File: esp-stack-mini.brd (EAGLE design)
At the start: 53.6 x 54.9 mm, 43 parts, among them IC1 FT232RL, Q1 200mA/50V, U1 TPS737XX, U2 MCP73831

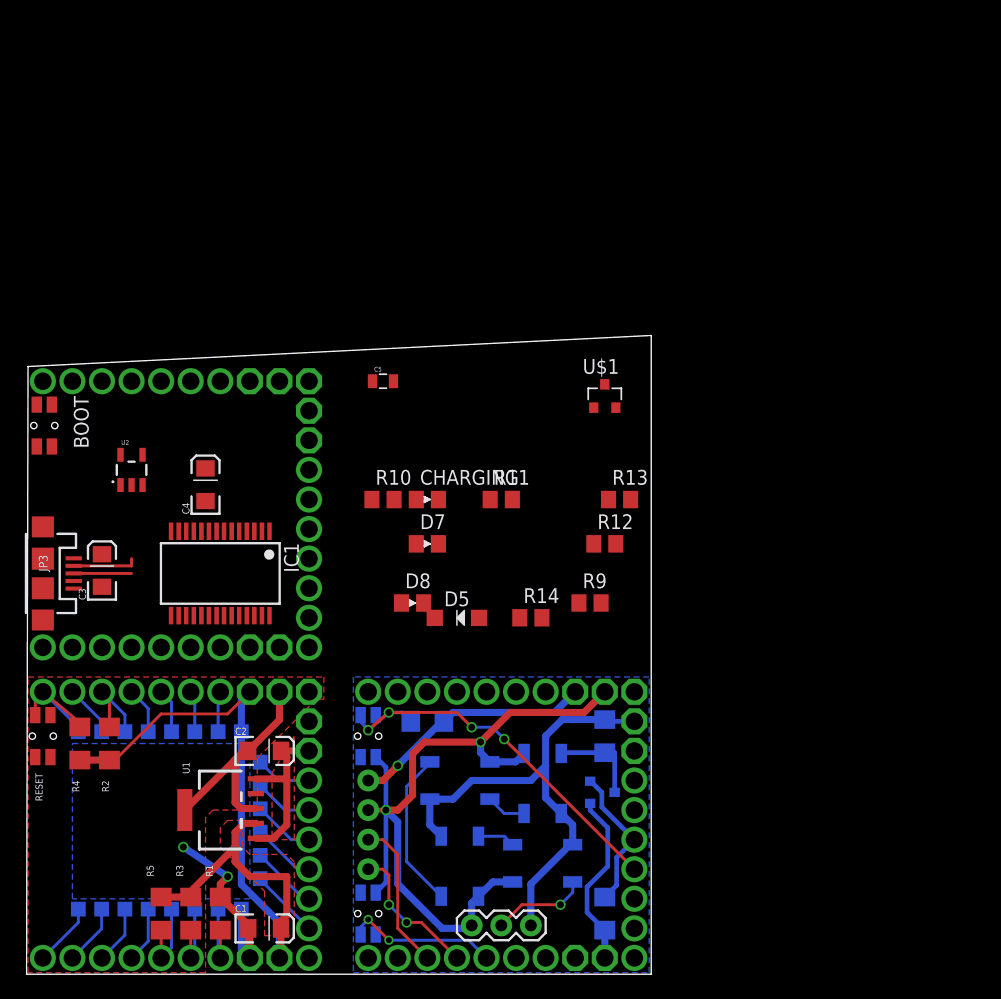
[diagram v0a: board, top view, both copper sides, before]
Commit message: USB/Battery board all-connected
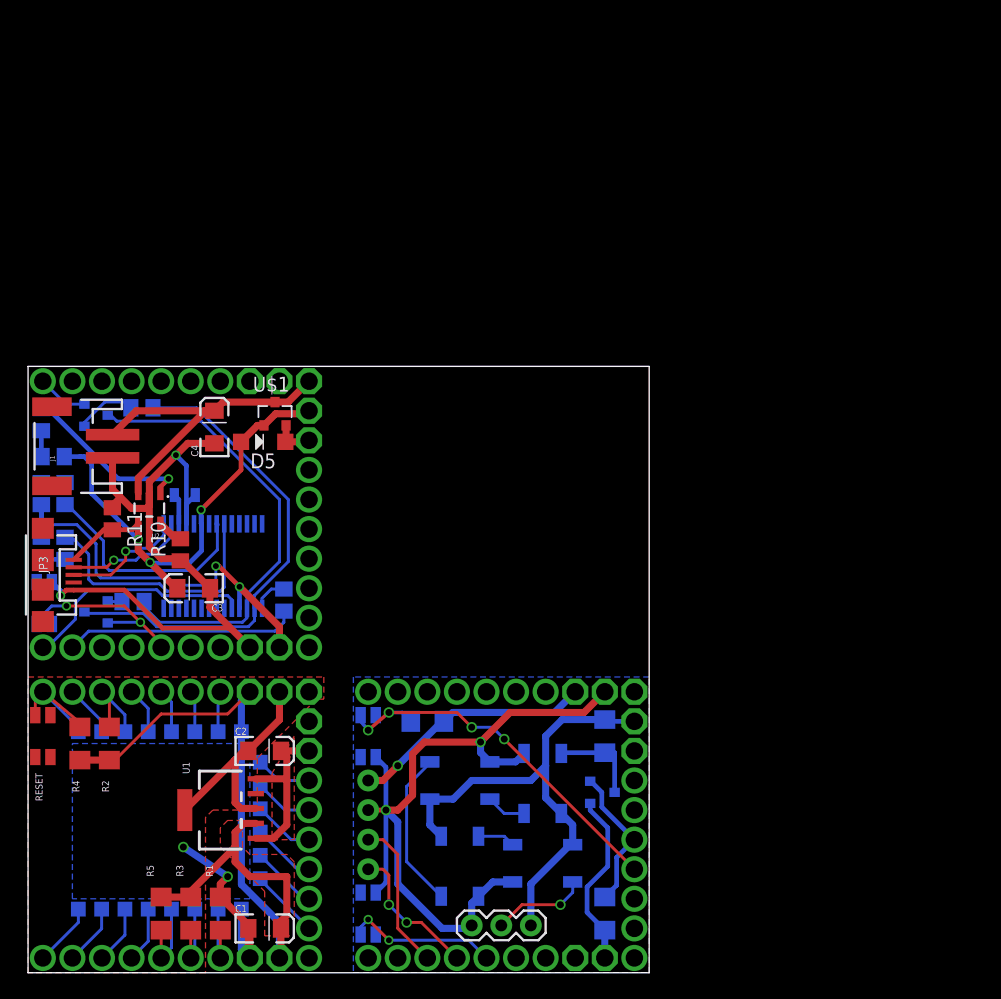
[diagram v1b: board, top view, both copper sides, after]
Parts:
- added J1: (no value), SparkFun-Connectors:JST-2-SMD
- added R15, R16: 12k, resistor:R0805
- added U$2, U$3: NPN-TRANSISTOR, ESPStack-mini:SOT23-3
- moved R9 47.8 mm to (2.16, 44.3), flipped to the bottom, turned to 180 degrees
- moved R13 47.6 mm to (3.17, 41.1), flipped to the bottom, turned to 270 degrees
- moved R12 46.4 mm to (3.17, 36.4), flipped to the bottom, turned to 90 degrees
- moved CHARGING 33.8 mm to (1.14, 47.5), flipped to the bottom, turned to 90 degrees
- moved R11 33.4 mm to (7.24, 39.0), turned to 270 degrees
- moved D8 33.2 mm to (1.14, 41.1), flipped to the bottom, turned to 90 degrees
- moved D7 33.1 mm to (1.14, 36.4), flipped to the bottom, turned to 270 degrees
- moved U$1 28.4 mm to (21.2, 48.0)
- moved D5 22.5 mm to (20.2, 45.6), turned to 180 degrees
- moved R14 21.3 mm to (22.0, 32.0), flipped to the bottom, turned to 90 degrees
- moved C5 19.6 mm to (13.5, 41.0), flipped to the bottom, turned to 180 degrees
- moved R10 17.9 mm to (13.1, 36.3), turned to 90 degrees
- moved BOOT 15.2 mm to (1.40, 31.8), flipped to the bottom, turned to 90 degrees
- moved C3 8.02 mm to (14.2, 33.0), turned to 180 degrees
- moved C4 5.01 mm to (16.0, 46.9)
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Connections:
- new net N$8: R16.1, U$3.1
- new net N$9: R15.1, U$2.1
- net D0: now also H3.D0, U$2.2
- net GND: now also BOOT.4, J1.1; no longer BOOT.3
- net N$15: now also R15.2, U$3.3
- net N$16: now also R16.2, U$2.3
- net RST: now also H3.RST, U$3.2
- net RX: now also H3.RX
- net TX: now also H3.TX
- net VBATT: now also J1.2
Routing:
- net GND: track 104.8 -> 166.7 mm, vias 4 -> 6
- net VBUS: track 41.9 -> 89.1 mm, vias 0 -> 3
- net N$16: track 0.00 -> 42.1 mm
- net N$15: track 0.00 -> 39.0 mm
- net 3V3: track 103.2 -> 138.7 mm, vias 1 -> 3
- net VBATT: track 0.00 -> 28.2 mm
- net N$17: track 0.00 -> 22.4 mm
- net TX: track 5.46 -> 25.7 mm
- net RX: track 5.23 -> 25.2 mm
- net N$18: track 0.00 -> 19.6 mm
- net D0: track 20.0 -> 36.0 mm, vias 2 -> 4
- net N$7: track 0.00 -> 15.0 mm, vias 0 -> 1
- net D+: track 4.97 -> 10.6 mm, vias 0 -> 1
- net N$8: track 0.00 -> 5.26 mm
- net D-: track 5.59 -> 10.6 mm, vias 0 -> 1
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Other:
- board size 53.6 x 54.9 mm -> 53.3 x 52.1 mm

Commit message: First prototype
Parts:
- removed U$2, U$3: NPN-TRANSISTOR, ESPStack-mini:SOT23-3
- added 1WIRE: (no value), SparkFun-Connectors:1X03
- added DHT11/22, HX711: (no value), SparkFun-Connectors:1X04_NO_SILK_ALL_ROUND
- added H4, H5, H6, H7, H8: ESP-BOARD, ESPStack-mini:ESP-BOARD
- added MODE: (no value), SparkFun-Retired:SJ_2
- added Q2: AO3401, ESPStack-mini:SOT23-3
- added Q3, Q4: S8050, ESPStack-mini:SOT23-3
- added R17, R18: 470, resistor:R0805
- added R19: 4k7, resistor:R0805
- added SJ1: SLEEP, jumper:SJ
- C5: value (none) -> 100nF
- D5: value SCHOTTKY_DIODE_SMDSOD123 -> MBR120
- D7: value DIODE_SMDD0805 -> TX
- D8: value DIODE_SMDD0805 -> RX
- Q1: value 200mA/50V -> BSS138
- R1, R2, R3, R4, R5, R6, R7, R8: device resistor:R1206 -> resistor:R0805
- U$1: value P-CHANNEL-MOSFET -> (none); device ESPStack-mini:SOT23-3 -> NBitWonder:OSHW1
- moved U$1 24.7 mm to (35.6, 27.9)
- moved D7 5.84 mm to (1.14, 42.3), turned to 90 degrees
- moved R12 5.84 mm to (3.17, 42.3), turned to 270 degrees
- moved R16 5.09 mm to (14.9, 48.8)
- moved C5 4.26 mm to (10.5, 38.0)
- moved IC1 4.02 mm to (17.1, 38.7), turned to 270 degrees
- moved D8 3.56 mm to (1.14, 37.6), turned to 270 degrees
- moved R13 3.56 mm to (3.17, 37.6), turned to 90 degrees
- moved R15 1.30 mm to (9.14, 33.2)
- moved BOOT 1.27 mm to (1.40, 33.0)
- moved C4 1.27 mm to (16.0, 48.1)
- moved CHARGING 1.27 mm to (1.14, 48.8)
- moved JP3 1.27 mm to (1.27, 35.4)
- moved R11 1.27 mm to (7.24, 40.3)
- moved R9 1.27 mm to (2.16, 45.6)
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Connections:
- new net 1WIRE: 1WIRE.2, MODE.3
- new net DHT: DHT11/22.2, MODE.1
- net 3V3: now also 1WIRE.1, DHT11/22.1, H4.3V3@1, H4.3V3@2, H5.3V3@1, H5.3V3@2, H6.3V3@1, H6.3V3@2, H7.3V3@1, H7.3V3@2, H8.3V3@1, H8.3V3@2, HX711.1, R19.2
- net ADC: now also H3.ADC, H6.ADC, H7.ADC, H8.ADC, R17.1, R18.2
- net D0: now also H6.D0, H7.D0, H8.D0, Q3.2; no longer U$2.2
- net D10: now also H6.D10, H7.D10, H8.D10; no longer B1.2, H2.D10, R6.1
- net D12: now also H4.D12, H6.D12, H7.D12, H8.D12, HX711.2
- net D13: now also H2.D13, H6.D13, H7.D13, H8.D13, Q1.2, R7.1
- net D14: now also H4.D14, H6.D14, H7.D14, H8.D14, HX711.3
- net D15: now also H5.D15, H6.D15, H7.D15, H8.D15, MODE.2, R19.1
- net D16: now also H3.D16, H6.D16, H7.D16, H8.D16, SJ1.2
- net D2: now also B1.2, H2.D2, H6.D2, H7.D2, H8.D2, R6.1
- net D4: now also H6.D4, H7.D4, H8.D4
- net D5: now also H6.D5, H7.D5, H8.D5
- net D9: now also H6.D9, H7.D9, H8.D9; no longer H2.D9, Q1.2, R7.1
- net GND: now also 1WIRE.3, DHT11/22.4, H4.GND@1, H4.GND@2, H5.GND@1, H5.GND@2, H6.GND@1, H6.GND@2, H7.GND@1, H7.GND@2, H8.GND@1, H8.GND@2, HX711.4, R18.1
- net N$15: now also Q4.3; no longer U$3.3
- net N$16: now also Q3.3; no longer U$2.3
- net N$8: now also Q4.1; no longer U$3.1
- net N$9: now also Q3.1; no longer U$2.1
- net RST: now also Q4.2, SJ1.1; no longer U$3.2
- net S1: now also H6.S1, H7.S1, H8.S1
- net V+: now also H4.V+, H5.V+, H6.V+, H7.V+, H8.V+, Q2.2; no longer U$1.2
- net VBATT: now also H4.VBATT, H5.VBATT, H6.VBATT, H7.VBATT, H8.VBATT, Q2.3, R17.2; no longer U$1.3
- net VBUS: now also H4.VBUS, H5.VBUS, H6.VBUS, H7.VBUS, H8.VBUS, Q2.1; no longer U$1.1
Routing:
- net GND: track 166.7 -> 289.1 mm, vias 6 -> 34
- net 3V3: track 138.7 -> 211.7 mm, vias 3 -> 10
- net D2: track 6.73 -> 50.6 mm, vias 0 -> 4
- net D13: track 3.51 -> 34.5 mm, vias 0 -> 4
- net D14: track 3.80 -> 30.3 mm, vias 0 -> 4
- net D12: track 3.57 -> 30.1 mm, vias 0 -> 3
- net D10: track 38.3 -> 16.3 mm, vias 4 -> 3
- net D9: track 17.9 -> 39.1 mm, vias 0 -> 3
- net D15: track 6.66 -> 23.5 mm, vias 0 -> 3
- net 1WIRE: track 0.00 -> 16.5 mm
- net RST: track 15.8 -> 30.5 mm
- net ADC: track 4.47 -> 19.0 mm, vias 0 -> 3
- net D16: track 4.02 -> 17.8 mm, vias 0 -> 3
- net TX: track 25.7 -> 38.0 mm
- net N$13: track 2.25 -> 13.2 mm
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- added copper zone on layer 1, net VBATT
- added copper zone on layer 1, net VBUS
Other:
- board size 53.3 x 52.1 mm -> 81.8 x 81.8 mm
- board text added: "ESP Stack mini"

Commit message: progress
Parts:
- R17: value 470 -> 220k
- R18: value 470 -> 51k
- R19: value 4k7 -> 9k1
- moved H6 35.9 mm to (81.3, 53.3), turned to 180 degrees
- moved U$1 7.73 mm to (27.9, 26.7)
- moved Q3 5.08 mm to (10.9, 32.4)
- moved Q4 4.73 mm to (13.7, 48.9), turned to 270 degrees
- moved MODE 3.83 mm to (66.0, 4.65), turned to 180 degrees
- moved R10 3.57 mm to (13.3, 41.1)
- moved R16 2.98 mm to (17.8, 49.4)
- moved R15 1.85 mm to (7.37, 32.7)
- moved R19 1.80 mm to (71.1, 3.81), turned to 0 degrees
- moved R8 1.27 mm to (49.6, 19.5)
- moved R18 1.11 mm to (7.62, 47.7), turned to 0 degrees
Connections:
- net D0: now also H5.D0, MODE.2, Q3.3, R19.1; no longer Q3.2
- net D15: no longer H5.D15, MODE.2, R19.1
- net N$15: now also Q4.2; no longer Q4.3
- net N$16: now also Q3.2; no longer Q3.3
- net RST: now also Q4.3; no longer Q4.2
- net V+: now also D1.1, D2.1, D3.1, D4.1, JP2.3, R8.2
- net VBUS: no longer D1.1, D2.1, D3.1, D4.1, JP2.3, R8.2
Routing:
- net GND: track 289.1 -> 213.3 mm, vias 34 -> 7
- net V+: track 18.4 -> 60.4 mm
- net VBUS: track 92.8 -> 51.2 mm
- net D9: track 39.1 -> 5.29 mm, vias 3 -> 0
- net 3V3: track 211.7 -> 189.5 mm, vias 10 -> 4
- net D15: track 23.5 -> 7.13 mm, vias 3 -> 0
- net NEOPIXEL: track 9.35 -> 21.2 mm, vias 0 -> 2
- net D14: track 30.3 -> 19.5 mm, vias 4 -> 1
- net S1: track 10.8 -> 0.00 mm, vias 3 -> 0
- net D16: track 17.8 -> 7.02 mm, vias 3 -> 0
- net D10: track 16.3 -> 5.51 mm, vias 3 -> 0
- net D12: track 30.1 -> 19.3 mm, vias 3 -> 0
- net D5: track 15.8 -> 5.01 mm, vias 3 -> 0
- net D4: track 15.6 -> 4.79 mm, vias 3 -> 0
- net D2: track 50.6 -> 39.8 mm, vias 4 -> 1
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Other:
- outline, holes or cut-outs redrawn
- board text added: "3V3"
- board text added: "SCL"
- board text added: "SDA"
- board text added: "breadboard adapter"
- board text added: "esp-12e"
- board text added: "rev 0.2"

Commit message: wip
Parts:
- removed 1WIRE: (no value), SparkFun-Connectors:1X03
- removed B1, B2: (no value), ESPStack-mini:SKSCLDE010
- removed CHARGING: DIODE_SMDD0805, diodes_gen:D0805
- removed D7: TX, diodes_gen:D0805
- removed D8: RX, diodes_gen:D0805
- removed J1: (no value), SparkFun-Connectors:JST-2-SMD
- removed MODE: (no value), SparkFun-Retired:SJ_2
- removed R12, R13: 10k, resistor:R0805
- added 1WIRE@1, 1WIRE@2: (no value), SparkFun-Connectors:1X03_NO_SILK
- added BATT: (no value), SparkFun-Connectors:1X02_NO_SILK
- added CHARG: DIODE_SMDD0805, diodes_gen:D0805
- added DHT-MODE-1WIRE: (no value), SparkFun-Retired:SJ_2
- added JP4: USB-A-H, SparkFun-Connectors:USB-A-H
- added JP5, JP6: (no value), SparkFun-Connectors:1X14
- added POWER, SKIP: (no value), jumper:SJ
- added U$2, U$3: POGO-PAD, ESPStack-mini:POGO-PAD
- added USB_BREAKOUT, USB_BREAKOUT1: (no value), SparkFun-Connectors:1X04_NO_SILK_ALL_ROUND
- JP2: device SparkFun-Connectors:1X03 -> SparkFun-Connectors:1X03_NO_SILK
- R19: value 9k1 -> 4k7*
- R6: value 10k -> 470
- moved RESET 98.0 mm to (80.0, 78.7), turned to 90 degrees
- moved R4 93.1 mm to (79.5, 74.8), turned to 180 degrees
- moved R2 90.7 mm to (76.5, 77.9), turned to 180 degrees
- moved R1 81.0 mm to (76.5, 59.5), turned to 180 degrees
- moved H1 79.0 mm to (55.9, 55.9)
- moved ESP-12E 78.7 mm to (75.6, 61.1)
- moved R3 78.3 mm to (70.4, 59.4), turned to 0 degrees
- moved R5 77.3 mm to (66.4, 59.4), turned to 180 degrees
- moved H4 55.9 mm to (0.00, 0.00)
- moved HX711 55.9 mm to (20.3, 8.89)
- moved R6 52.5 mm to (4.06, 64.8), flipped to the top, turned to 90 degrees
- moved BOOT 50.8 mm to (24.0, 78.5), flipped to the top
- moved H6 35.9 mm to (55.9, 27.9), turned to 0 degrees
- moved C1 34.9 mm to (17.5, 38.6)
- moved R14 33.1 mm to (5.26, 60.6), flipped to the top, turned to 90 degrees
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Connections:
- removed net S1: H1.S1, H6.S1, H7.S1, H8.S1
- new net N$40: H6.D0, JP5.5
- new net N$52: H6.D2, JP5.6
- new net N$58: H6.D15, JP5.7
- new net N$65: H6.RST, JP6.14
- new net N$66: H6.ADC, JP6.13
- new net N$67: H6.EN, JP6.12
- new net N$68: H6.D16, JP6.11
- new net N$69: H6.D14, JP6.10
- new net N$70: H6.D12, JP6.9
- new net N$71: H6.D13, JP6.8
- new net NEOPIXEL_EXTERNAL: D4.2, JP2.2, SKIP.2
- new net NEOPIXEL_VCC: D1.1, D2.1, D3.1, D4.1, JP2.3, POWER.1, R8.2
- new net VBAT: H6.VBATT, JP5.13
- net 1WIRE: now also 1WIRE@1.2, 1WIRE@2.2, DHT-MODE-1WIRE.3; no longer 1WIRE.2, MODE.3
- net 3V3: now also 1WIRE@1.1, 1WIRE@2.1, C2.A, JP5.8, JP6.7; no longer 1WIRE.1, C1.A, D7.A, D8.A, R6.2
- net ADC: no longer H6.ADC, H8.ADC
- net CS0: now also H6.CS0, JP6.3
- net D+: now also JP4.D+, U$3.P$2, USB_BREAKOUT.2, USB_BREAKOUT1.2
- net D-: now also JP4.D-, U$2.P$2, USB_BREAKOUT.3, USB_BREAKOUT1.3
- net D0: now also DHT-MODE-1WIRE.2; no longer B2.1, H6.D0, MODE.2
- net D10: no longer H1.D10, H6.D10, H7.D10, H8.D10
- net D12: now also H5.D12; no longer H6.D12, H8.D12
- net D13: now also H5.D13; no longer H6.D13, H8.D13
- net D14: now also H5.D14; no longer H6.D14, H8.D14
- net D15: now also H5.D15; no longer H6.D15, H8.D15
- net D16: now also H5.D16; no longer H6.D16, H8.D16
- net D2: now also H5.D2; no longer B1.2, H6.D2, H8.D2, R6.1
- net D4: now also H5.D4; no longer H6.D4, H8.D4
- net D5: now also H5.D5; no longer H6.D5, H8.D5
- net D9: no longer H1.D9, H6.D9, H7.D9, H8.D9
- net DHT: now also DHT-MODE-1WIRE.1; no longer MODE.1
- net GND: now also 1WIRE@1.3, 1WIRE@2.3, BATT.2, JP4.GND, JP5.14, JP5.9, JP6.1, JP6.2, JP6.6, USB_BREAKOUT.1, USB_BREAKOUT1.1; no longer 1WIRE.3, B1.3, B2.4, J1.1
- net MISO: now also H6.MISO, JP6.4
- net MOSI: now also H6.MOSI, JP6.5
- net N$17: now also H6.TX, JP5.1; no longer IC1.23, R12.2
- net N$18: now also H6.RX, JP5.2; no longer IC1.22, R13.2
- net N$19: now also H6.D5, JP5.3; no longer D7.K, R12.1
- net N$20: now also H6.D4, JP5.4; no longer D8.K, R13.1
- net N$4: now also IC1.5, R6.2; no longer D4.2, JP2.2
- net N$6: now also CHARG.A; no longer CHARGING.A
- net N$7: now also CHARG.K; no longer CHARGING.K
- net NEOPIXEL: now also SKIP.1
- net RST: now also H8.RST
- net RX: now also H8.RX
- net SCLK: now also H6.SCLK, JP5.10
- net TX: now also H8.TX, R6.1; no longer IC1.5
- net V+: now also C1.A, JP5.11, POWER.2; no longer C2.A, D1.1, D2.1, D3.1, D4.1, JP2.3, R8.2
- net VBATT: now also BATT.1; no longer H6.VBATT, J1.2
- net VBUS: now also JP4.VBUS, JP5.12, USB_BREAKOUT.4, USB_BREAKOUT1.4
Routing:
- net GND: track 213.3 -> 361.3 mm, vias 7 -> 39
- net 3V3: track 189.5 -> 281.6 mm, vias 4 -> 6
- net NEOPIXEL_VCC: track 0.00 -> 52.7 mm
- net VBUS: track 51.2 -> 98.6 mm, vias 3 -> 2
- net D2: track 39.8 -> 6.80 mm
- net N$65: track 0.00 -> 31.9 mm
- net N$67: track 0.00 -> 30.5 mm
- net N$71: track 0.00 -> 30.5 mm
- net N$69: track 0.00 -> 30.5 mm
- net N$66: track 0.00 -> 30.5 mm
- net N$58: track 0.00 -> 30.5 mm
- net N$40: track 0.00 -> 30.5 mm, vias 1 -> 0
- net N$70: track 0.00 -> 30.5 mm
- net N$68: track 0.00 -> 30.5 mm
- net N$52: track 0.00 -> 30.5 mm, vias 1 -> 0
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- removed copper zone on layer 1, net 3V3
- removed copper zone on layer 1, net V+
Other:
- outline, holes or cut-outs redrawn
- board text added: "5V"
- board text added: "D0"
- board text added: "D12"
- board text added: "D13"
- board text added: "D14"
- board text added: "D15"
- board text added: "D16"
- board text added: "D2"
- board text added: "D4"
- board text added: "D5"
- board text added: "DOUT"
- board text added: "TOP"
- board text removed: "DIN"
- board text removed: "VBUS"
- board text removed: "breadboard adapter"
- board text removed: "esp-12e"
